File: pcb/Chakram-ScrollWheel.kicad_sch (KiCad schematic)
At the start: 16 parts, among them J1 FPC Connector, SW1 RotaryEncoder

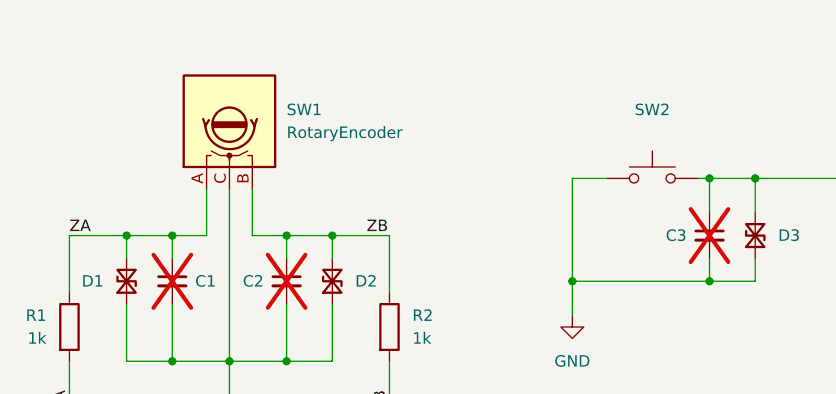
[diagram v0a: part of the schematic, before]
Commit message: Improved encoder symbol to also include  MP pins and connected them to GND
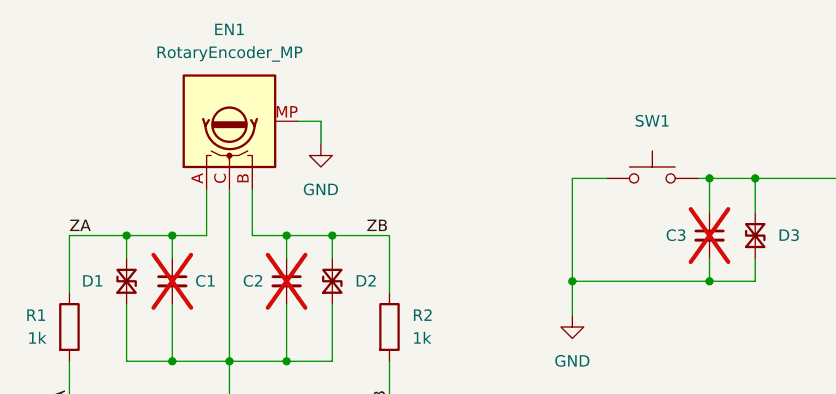
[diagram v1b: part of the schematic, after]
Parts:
- EN1: renamed from SW1; value RotaryEncoder -> RotaryEncoder_MP; footprint Moucha_Primitives:RotaryEncoder_Alps_EC10E -> (none); symbol Device:RotaryEncoder -> Moucha_Mechanical:RotaryEncoder_MP
- renumbered SW2 to SW1
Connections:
- net GND: now also EN1.MP
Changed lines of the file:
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@@
+	(wire
+		(pts
+			(xy 64.77 55.88) (xy 67.31 55.88)
+		)
+		(stroke
+			(width 0)
+			(type default)
+		)
+	)
 	(wire
 		(pts
@@
 		(pts
 			(xy 109.22 62.23) (xy 110.49 62.23)
+		)
+		(stroke
+			(width 0)
+			(type default)
+		)
+	)
+	(wire
+		(pts
+			(xy 67.31 55.88) (xy 67.31 58.42)
 		)
 		(stroke
@@
 		(dnp no)
 		(fields_autoplaced yes)
-		(property "Reference" "SW2"
-			(at 104.14 54.61 0)
+		(property "Reference" "SW1"
+			(at 104.14 55.88 0)
 			(effects
 				(font
@@
 			(project ""
 				(path "/b09dc29a-b779-491f-be6b-b7a621e0664e"
-					(reference "SW2")
+					(reference "SW1")
 					(unit 1)
 				)
@@
 	)
 	(symbol
+		(lib_id "power:GND")
+		(at 67.31 58.42 0)
+		(unit 1)
+		(exclude_from_sim no)
+		(in_bom yes)
+		(on_board yes)
+		(dnp no)
+		(fields_autoplaced yes)
+		(property "Reference" "#PWR08"
+			(at 67.31 64.77 0)
+			(effects
+				(font
+					(size 1.27 1.27)
+				)
+				(hide yes)
+			)
+		)
+		(property "Value" "GND"
+			(at 67.31 63.5 0)
+			(effects
+				(font
+					(size 1.27 1.27)
+				)
+			)
+		)
+		(property "Footprint" ""
+			(at 67.31 58.42 0)
+			(effects
+				(font
+					(size 1.27 1.27)
+				)
+				(hide yes)
+			)
+		)
+		(property "Datasheet" ""
+			(at 67.31 58.42 0)
+			(effects
+				(font
+					(size 1.27 1.27)
+				)
+				(hide yes)
+			)
+		)
+		(property "Description" "Power symbol creates a global label with name \"GND\" , ground"
+			(at 67.31 58.42 0)
+			(effects
+				(font
+					(size 1.27 1.27)
+				)
+				(hide yes)
+			)
+		)
+		(pin "1"
+		)
+		(instances
+			(project "Chakram-ScrollWheel"
+				(path "/b09dc29a-b779-491f-be6b-b7a621e0664e"
+					(reference "#PWR08")
+					(unit 1)
+				)
+			)
+		)
+	)
+	(symbol
 		(lib_id "power:VDD")
 		(at 180.34 58.42 0)
@@
 	)
 	(symbol
-		(lib_id "Device:RotaryEncoder")
+		(lib_id "Moucha_Mechanical:RotaryEncoder_MP")
 		(at 57.15 55.88 90)
 		(unit 1)
@@
 		(dnp no)
 		(fields_autoplaced yes)
-		(property "Reference" "SW1"
-			(at 63.5 54.6099 90)
-			(effects
-				(font
-					(size 1.27 1.27)
-				)
-				(justify right)
-			)
-		)
-		(property "Value" "RotaryEncoder"
-			(at 63.5 57.1499 90)
-			(effects
-				(font
-					(size 1.27 1.27)
-				)
-				(justify right)
-			)
-		)
-		(property "Footprint" "Moucha_Primitives:RotaryEncoder_Alps_EC10E"
+		(property "Reference" "EN1"
+			(at 57.15 45.72 90)
+			(effects
+				(font
+					(size 1.27 1.27)
+				)
+			)
+		)
+		(property "Value" "RotaryEncoder_MP"
+			(at 57.15 48.26 90)
+			(effects
+				(font
+					(size 1.27 1.27)
+				)
+			)
+		)
+		(property "Footprint" ""
 			(at 53.086 59.69 0)
 			(effects
@@
 		)
 		(property "Datasheet" "~"
-			(at 50.546 55.88 0)
-			(effects
-				(font
-					(size 1.27 1.27)
-				)
-				(hide yes)
-			)
-		)
-		(property "Description" "Rotary encoder, dual channel, incremental quadrate outputs"
-			(at 57.15 55.88 0)
+			(at 69.85 55.88 0)
+			(effects
+				(font
+					(size 1.27 1.27)
+				)
+				(hide yes)
+			)
+		)
+		(property "Description" "Rotary encoder, dual channel, incremental quadrate outputs, with MP Pin"
+			(at 72.39 55.88 0)
 			(effects
 				(font
@@
 		)
 		(pin "B"
+		)
+		(pin "MP"
 		)
 		(instances
 			(project ""
 				(path "/b09dc29a-b779-491f-be6b-b7a621e0664e"
-					(reference "SW1")
+					(reference "EN1")
 					(unit 1)
 				)

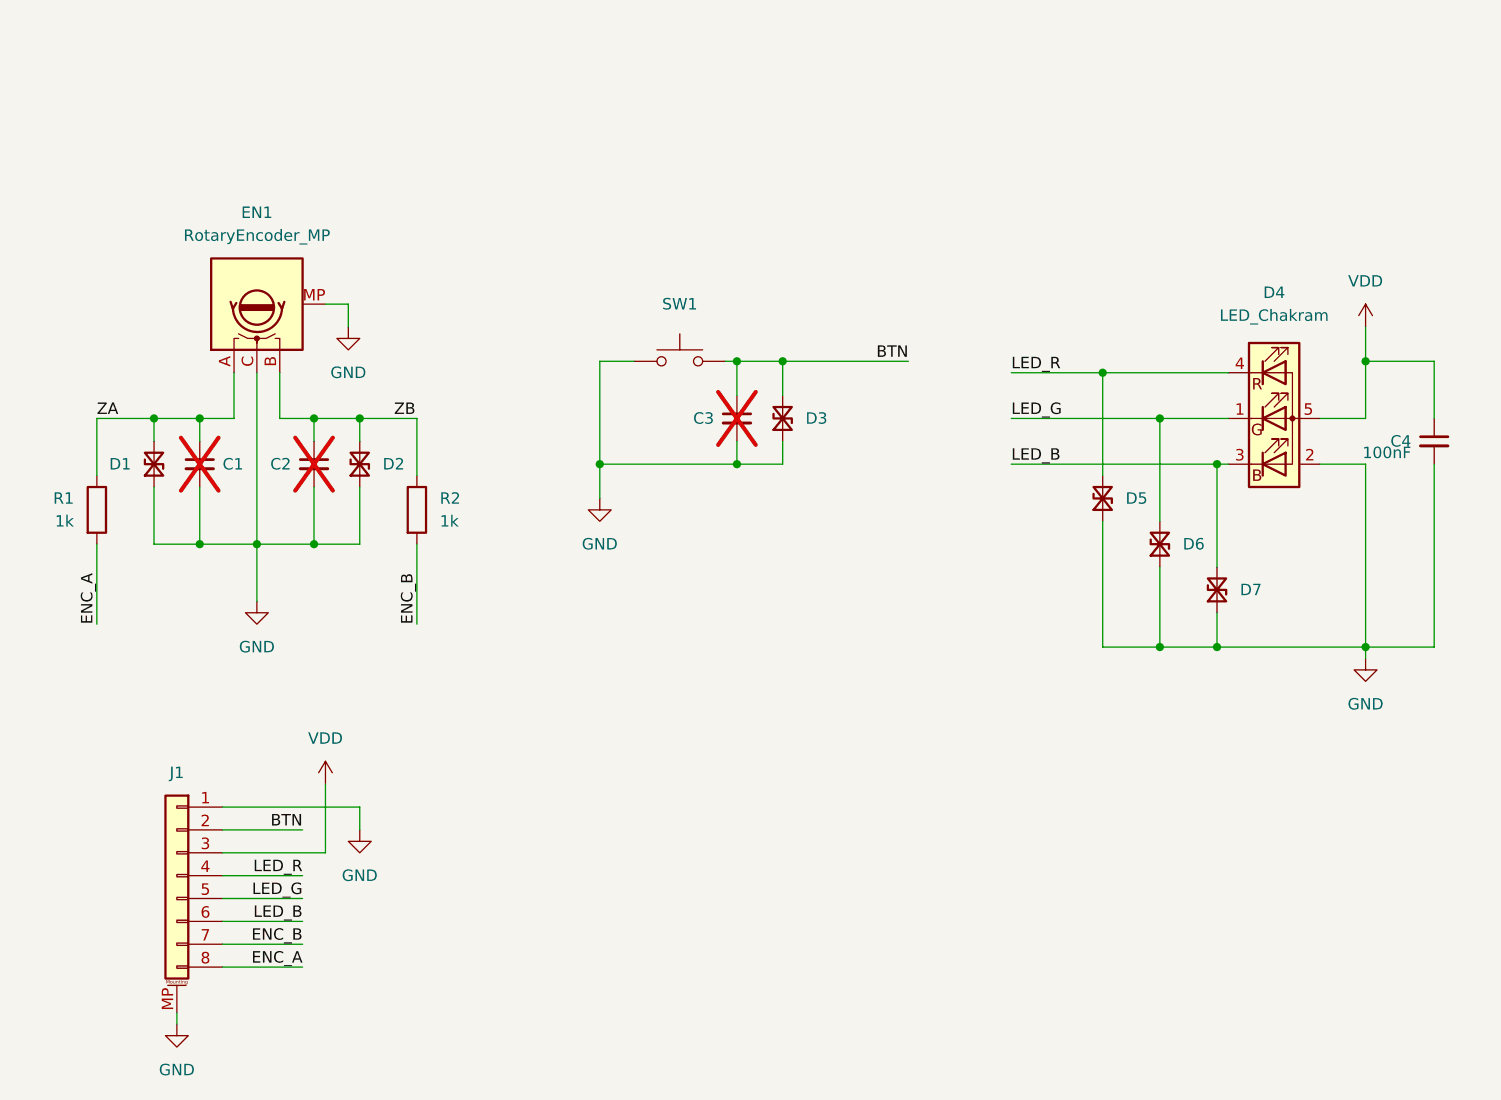
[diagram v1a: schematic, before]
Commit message: Added testpoints
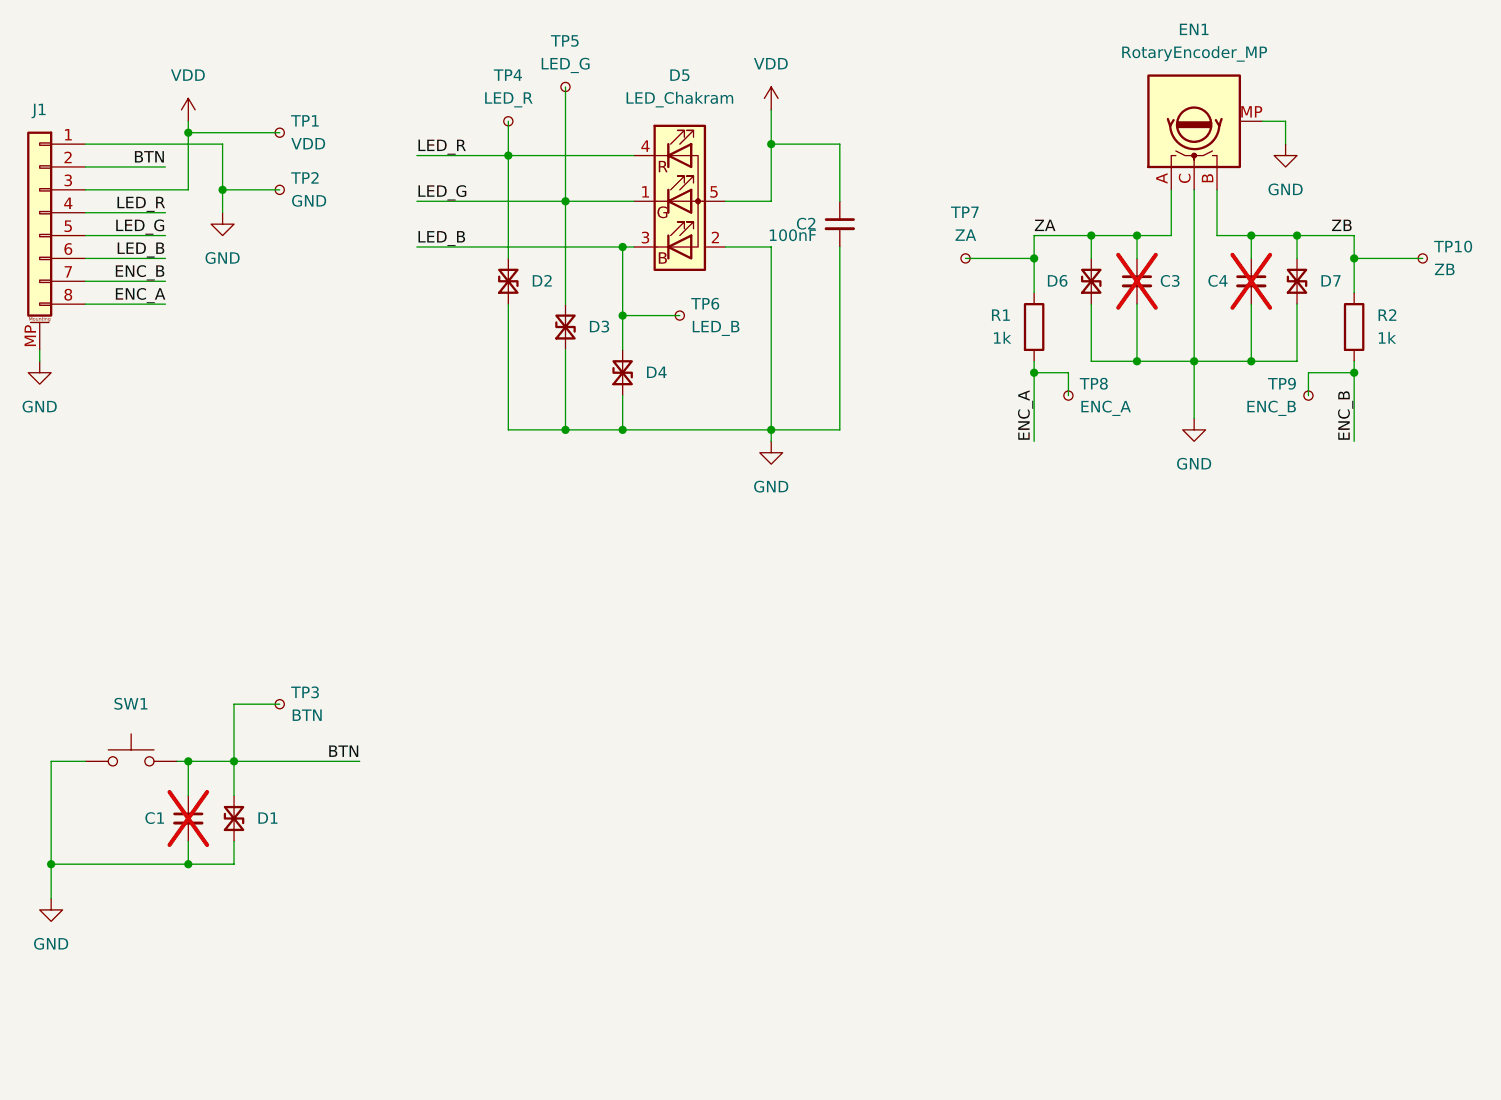
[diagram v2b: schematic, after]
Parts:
- added TP1: VDD, TestPoint:TestPoint_Pad_D1.0mm, symbol Connector:TestPoint_Small
- added TP10: ZB, TestPoint:TestPoint_Pad_D1.0mm, symbol Connector:TestPoint_Small
- added TP2: GND, TestPoint:TestPoint_Pad_D1.0mm, symbol Connector:TestPoint_Small
- added TP3: BTN, TestPoint:TestPoint_Pad_D1.0mm, symbol Connector:TestPoint_Small
- added TP4: LED_R, TestPoint:TestPoint_Pad_D1.0mm, symbol Connector:TestPoint_Small
- added TP5: LED_G, TestPoint:TestPoint_Pad_D1.0mm, symbol Connector:TestPoint_Small
- added TP6: LED_B, TestPoint:TestPoint_Pad_D1.0mm, symbol Connector:TestPoint_Small
- added TP7: ZA, TestPoint:TestPoint_Pad_D1.0mm, symbol Connector:TestPoint_Small
- added TP8: ENC_A, TestPoint:TestPoint_Pad_D1.0mm, symbol Connector:TestPoint_Small
- added TP9: ENC_B, TestPoint:TestPoint_Pad_D1.0mm, symbol Connector:TestPoint_Small
- renumbered C3 to C1, C4 to C2, C1 to C3, C2 to C4, D3 to D1, D5 to D2, D6 to D3, D7 to D4, D4 to D5, D1 to D6, D2 to D7
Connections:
- net BTN: now also TP3.1
- net ENC_A: now also TP8.1
- net ENC_B: now also TP9.1
- net GND: now also TP2.1
- net LED_B: now also TP6.1
- net LED_G: now also TP5.1
- net LED_R: now also TP4.1
- net VDD: now also TP1.1
- net ZA: now also TP7.1
- net ZB: now also TP10.1
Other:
- moved on the sheet: C1, C2, C3, C4, D1, D2, D3, D4, D5, D6, D7, EN1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

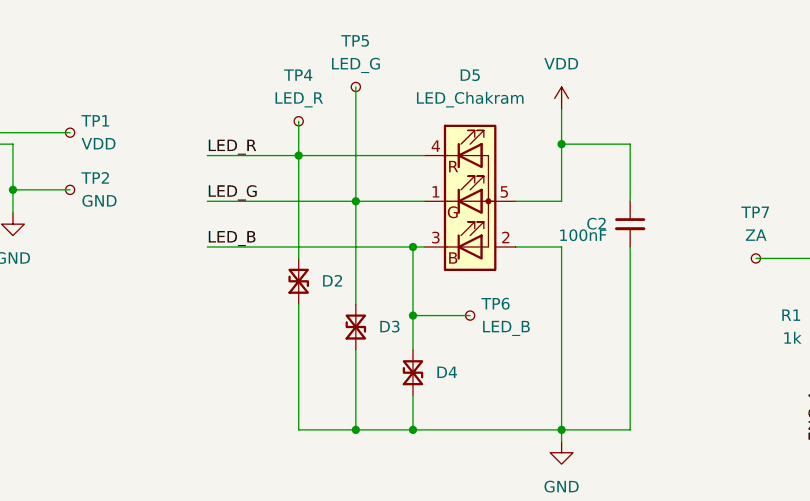
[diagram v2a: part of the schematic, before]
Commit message: Positioned all test points
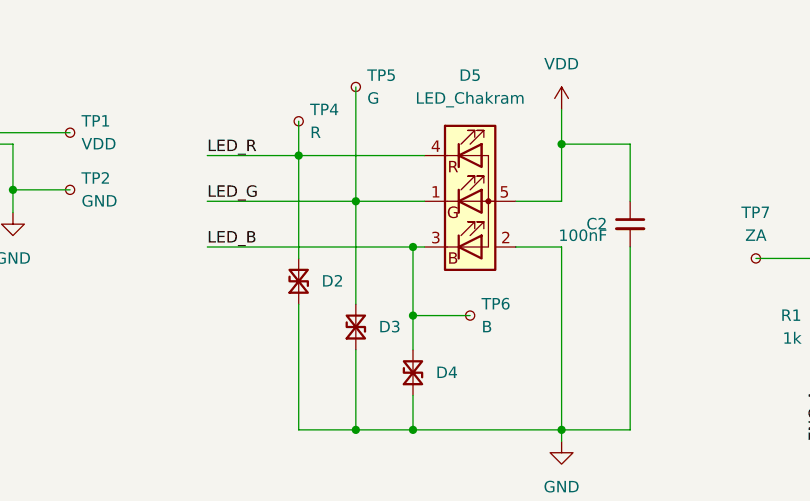
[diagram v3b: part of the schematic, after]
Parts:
- TP4: value LED_R -> R
- TP5: value LED_G -> G
- TP6: value LED_B -> B
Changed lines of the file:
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@@
 		(fields_autoplaced yes)
 		(property "Reference" "TP5"
-			(at 91.44 26.67 0)
-			(effects
-				(font
-					(size 1.27 1.27)
-				)
-			)
-		)
-		(property "Value" "LED_G"
-			(at 91.44 29.21 0)
-			(effects
-				(font
-					(size 1.27 1.27)
-				)
+			(at 92.71 30.4799 0)
+			(effects
+				(font
+					(size 1.27 1.27)
+				)
+				(justify left)
+			)
+		)
+		(property "Value" "G"
+			(at 92.71 33.0199 0)
+			(effects
+				(font
+					(size 1.27 1.27)
+				)
+				(justify left)
 			)
 		)
@@
 		(fields_autoplaced yes)
 		(property "Reference" "TP4"
-			(at 85.09 30.48 0)
-			(effects
-				(font
-					(size 1.27 1.27)
-				)
-			)
-		)
-		(property "Value" "LED_R"
-			(at 85.09 33.02 0)
-			(effects
-				(font
-					(size 1.27 1.27)
-				)
+			(at 86.36 34.2899 0)
+			(effects
+				(font
+					(size 1.27 1.27)
+				)
+				(justify left)
+			)
+		)
+		(property "Value" "R"
+			(at 86.36 36.8299 0)
+			(effects
+				(font
+					(size 1.27 1.27)
+				)
+				(justify left)
 			)
 		)
@@
 			)
 		)
-		(property "Value" "LED_B"
+		(property "Value" "B"
 			(at 105.41 58.4199 0)
 			(effects

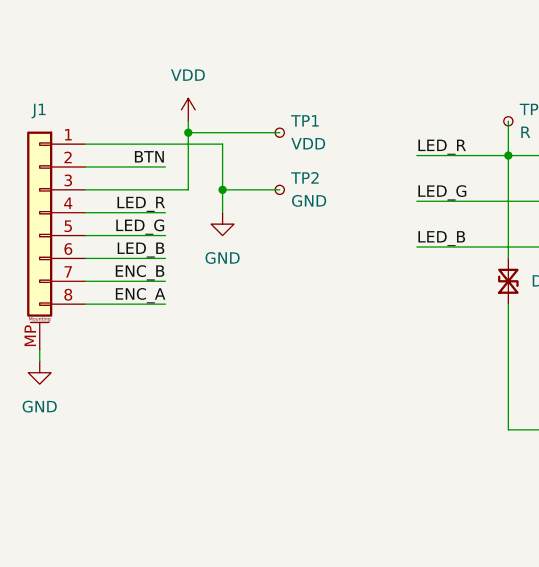
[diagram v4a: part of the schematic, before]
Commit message: Fixed swapped ENC_A and ENC_B signals on J1
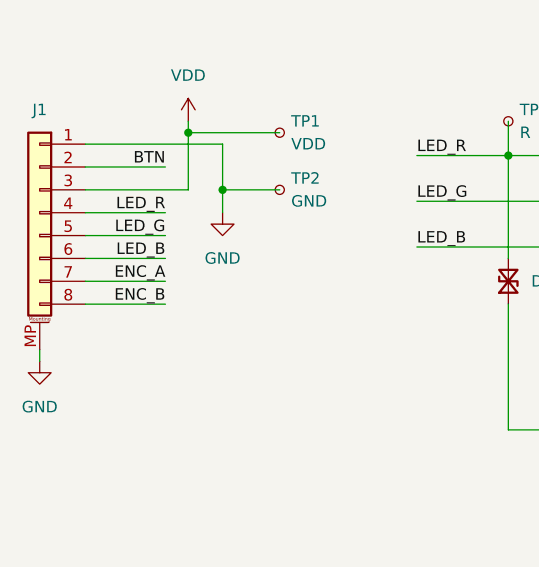
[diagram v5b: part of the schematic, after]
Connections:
- net ENC_A: now also J1.7 (Pin_7); no longer J1.8 (Pin_8)
- net ENC_B: now also J1.8 (Pin_8); no longer J1.7 (Pin_7)
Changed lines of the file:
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@@
 		)
 	)
-	(label "ENC_A"
+	(label "ENC_B"
 		(at 46.99 55.88 180)
 		(fields_autoplaced yes)
@@
 		)
 	)
-	(label "ENC_B"
+	(label "ENC_A"
 		(at 46.99 53.34 180)
 		(fields_autoplaced yes)
